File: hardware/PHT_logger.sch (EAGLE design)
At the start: 14 parts, among them IC3 ESP32-S3-WROOM-1-N16R2

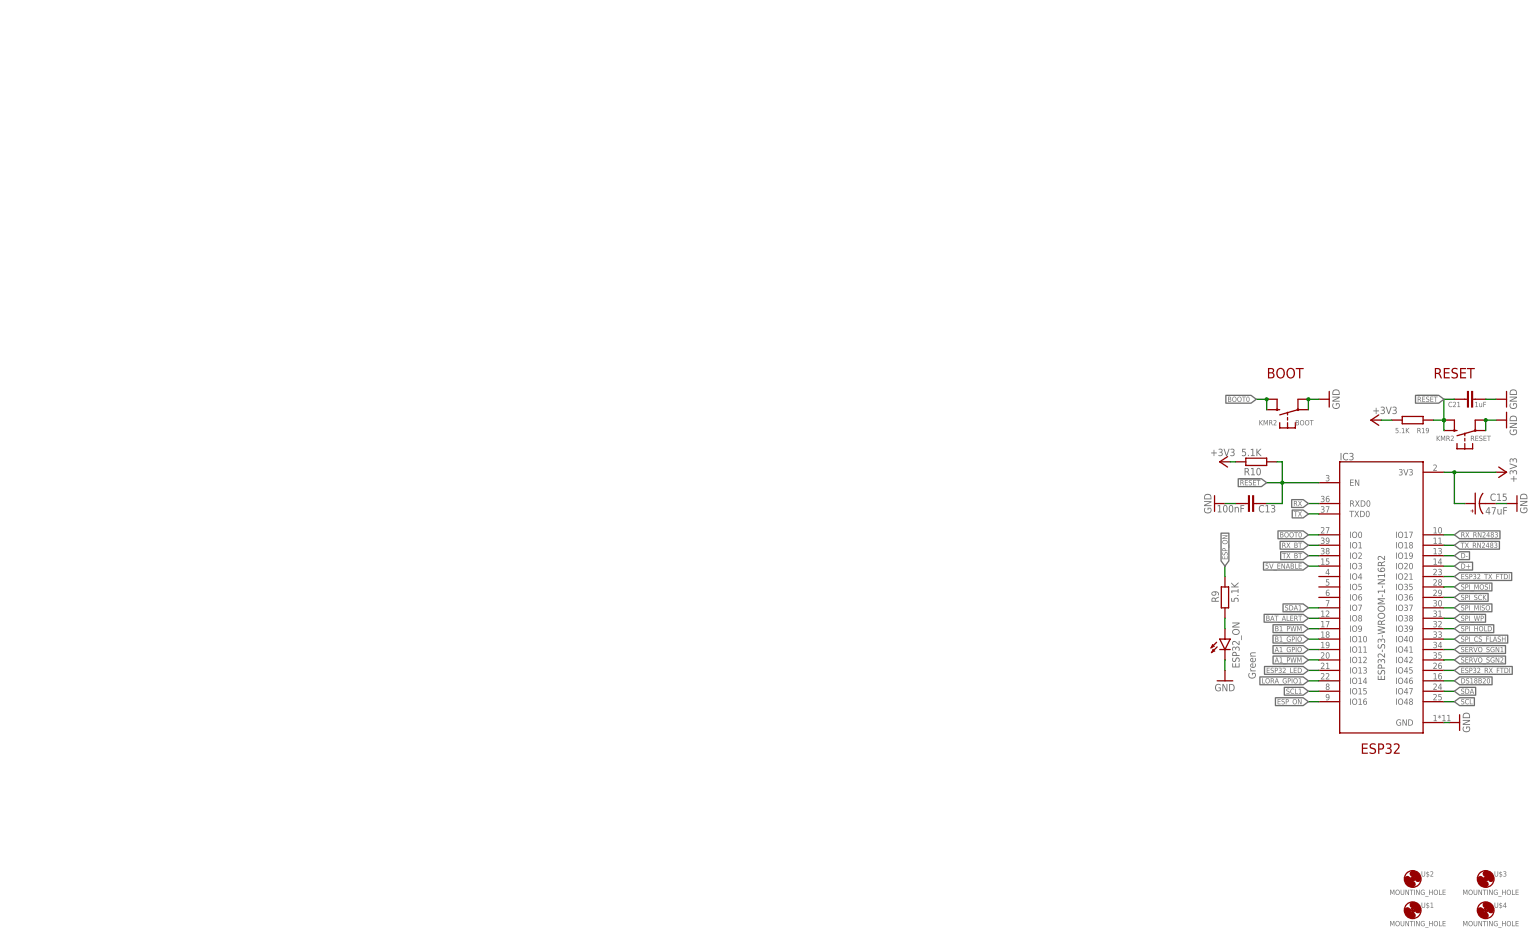
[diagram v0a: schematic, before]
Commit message: Powe components updated on schematics
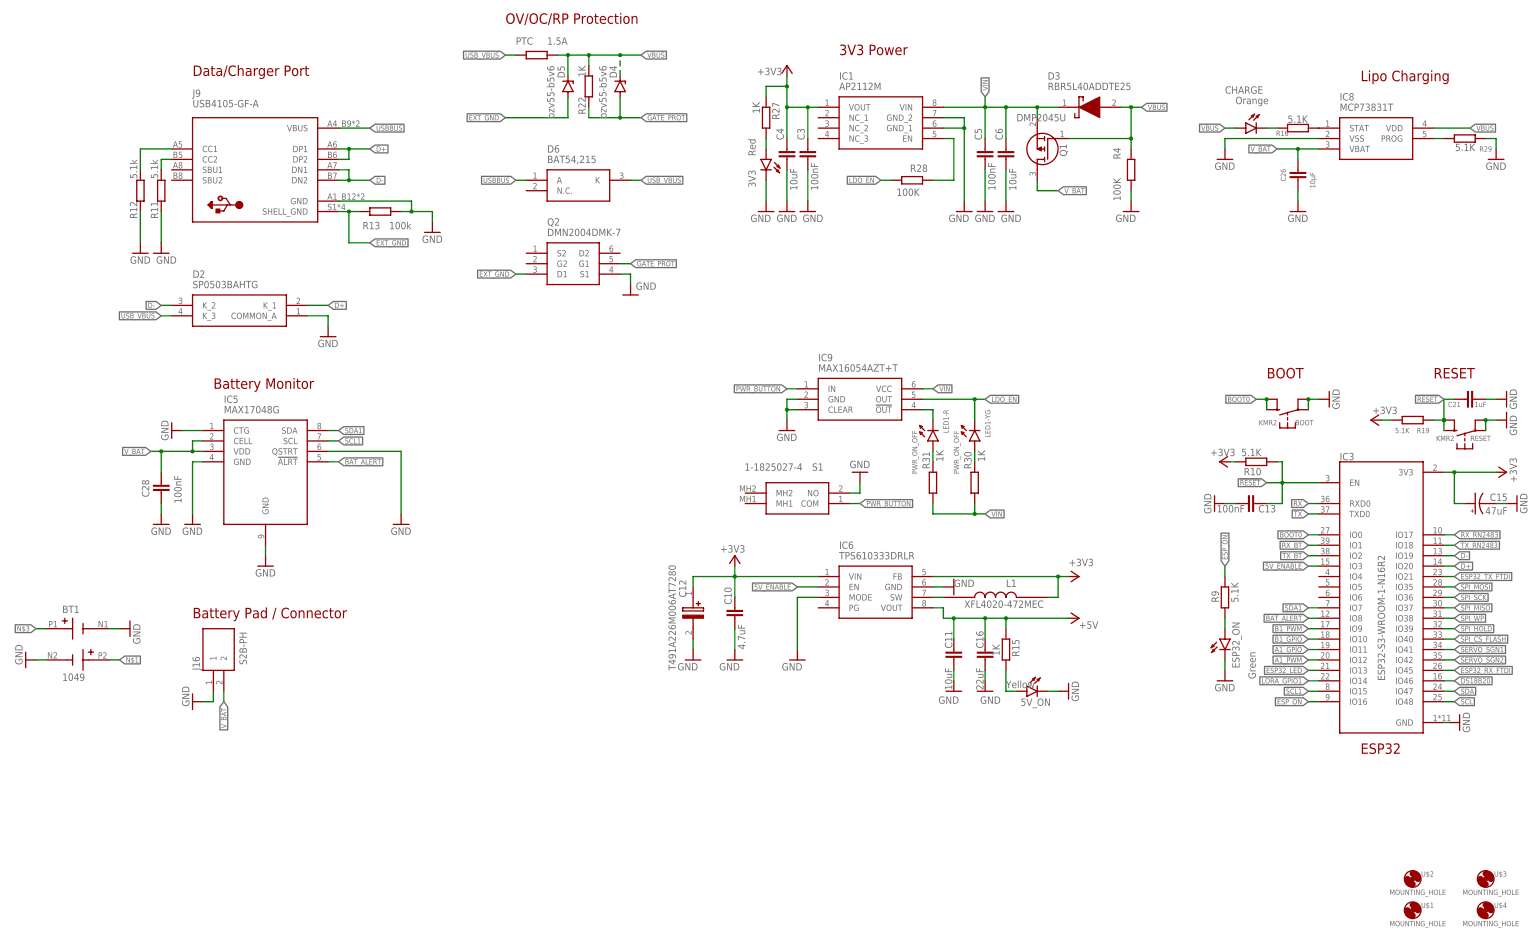
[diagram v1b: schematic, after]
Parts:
- added 3V3: Red, led:LEDCHIPLED_0805
- added 5V_ON: Yellow, led:LEDCHIPLED_0805
- added BT1: 1049, 1049:1049
- added C10: 4.7uF, rcl:C-EUC0805
- added C11: 10uF, rcl:C-EUC0805
- added C12: T491A226M006AT7280, T491A226M006AT7280:T491A226M006AT7280
- added C16: 22uF, rcl:C-EUC0805
- added C26: 10µF, rcl:C-EUC0603K
- added C28, C3, C5: 100nF, rcl:C-EUC0603
- added C4, C6: 10uF, rcl:C-EUC0603
- added CHARGE: Orange, led:LEDCHIPLED_0805
- added D2: SP0503BAHTG, SP0503BAHTG:SP0503BAHTG
- added D3: RBR5L40ADDTE25, RBR5L40ADDTE25:RBR5L40ADDTE25
- added D4, D5: bzv55-b5v6, diode:ZENER-DIODESOD80C
- added D6: BAT54,215, BAT54_215:BAT54,215
- added IC1: AP2112M, AP2112M-3.3TRG1:AP2112M-3.3TRG1
- added IC5: MAX17048G, MAX17048G+T10:MAX17048G+T10
- added IC6: TPS610333DRLR, TPS610333DRLR:TPS610333DRLR
- added IC8: MCP73831T, MCP73831T-2ACI_OT:MCP73831T-2ACI_OT
- added IC9: MAX16054AZT+T, MAX16054AZT+T:MAX16054AZT+T
- added J16: S2B-PH, S2B-PH-K-S_LF__SN_:S2B-PH-K-S(LF)(SN)
- added J9: USB4105-GF-A, USB4105-GF-A:USB4105-GF-A
- added L1: XFL4020-472MEC, XFL4020-472MEC:XFL4020-472MEC
- added LED1: PWR_ON_OFF, OSRG1206C1C:OSRG1206C1C
- added PTC: 1.5A, rcl:R-EU_R2512
- added Q1: DMP2045U, DMP2045U-7:DMP2045U-7
- added Q2: DMN2004DMK-7, DMN2004DMK-7:DMN2004DMK-7
- added R11, R12: 5.1k, rcl:R-EU_R0603
- added R13: 100k, rcl:R-EU_R0603
- added R15, R22, R27, R30, R31: 1K, rcl:R-EU_R0603
- added R16, R29: 5.1K, rcl:R-EU_R0603
- added R28, R4: 100K, rcl:R-EU_R0603
- added S1: 1-1825027-4, 1-1825027-4:1-1825027-4
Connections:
- new net +5V: C11.2, C16.2, IC6.VOUT, R15.1
- new net EXT_GND: D5.A, J9.SHELL_GND, Q2.D1, R13.2
- new net GATE_PROT: D4.A, Q2.G1, R22.1
- new net LDO_EN: IC9.OUT, LED1-YG.C, R28.1
- new net N$1: BT1.POS2
- new net N$10: 5V_ON.A, R15.2
- new net N$11: CHARGE.C, R16.1
- new net N$12: IC9.!OUT, LED1-R.C
- new net N$13: IC1.EN, R28.2
- new net N$14: LED1-YG.A, R30.2
- new net N$15: LED1-R.A, R31.2
- new net N$16: J9.CC2, R11.2
- new net N$17: IC8.STAT, R16.2
- new net N$18: IC8.PROG, R29.2
- new net N$21: J9.CC1, R12.2
- new net N$3: BT1.POS1
- new net N$33: 3V3.A, R27.2
- new net N$9: IC6.SW, L1.1
- new net PWR_BUTTON: IC9.IN, S1.COM
- new net USBBUS: D6.A, J9.VBUS
- new net USB_VBUS: D2.K_3, D6.K, PTC.1
- new net VBUS: CHARGE.A, D3.A, D4.C, D5.C, IC8.VDD, PTC.2, Q1.G, R22.2, R4.1
- new net VIN: C5.2, C6.2, D3.K, IC1.VIN, IC9.VCC, Q1.S, R30.1, R31.1
- new net V_BAT: C26.1, C28.1, IC5.CELL, IC5.VDD, IC8.VBAT, J16.2, Q1.D
- net +3V3: now also C10.2, C12.+, C3.2, C4.2, IC1.VOUT, IC6.FB, IC6.VIN, L1.2, R27.1
- net 5V_ENABLE: now also IC6.EN
- net BAT_ALERT: now also IC5.!ALRT
- net D+: now also D2.K_1, J9.DP1, J9.DP2
- net D-: now also D2.K_2, J9.DN1, J9.DN2
- net GND: now also 3V3.C, 5V_ON.C, BT1.NEG1, BT1.NEG2, C10.1, C11.1, C12.-, C16.1, C26.2, C28.2, C3.1, C4.1, C5.1, C6.1, D2.COMMON_A, IC1.GND_1, IC1.GND_2, IC5.CTG, IC5.GND, IC5.GND@, IC5.QSTRT, IC6.GND, IC6.MODE, IC8.VSS, IC9.CLEAR, IC9.GND, J16.1, J9.GND, Q2.S1, R11.1, R12.1, R13.1, R29.1, R4.2, S1.NO
- net SCL1: now also IC5.SCL
- net SDA1: now also IC5.SDA
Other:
- note added: "3V3 Power"
- note added: "Battery Monitor"
- note added: "Battery Pad / Connector"
- note added: "Data/Charger Port"
- note added: "Lipo Charging"
- note added: "OV/OC/RP Protection"
